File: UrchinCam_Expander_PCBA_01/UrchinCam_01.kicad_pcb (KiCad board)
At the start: 4 copper layers, 31.5 x 65 mm, 86 parts, among them J1 95157-440LF, J2 SM04B-GHS, J3 SM04B-GHS, J4 SM02B-GHS, J5 Conn_01x04_Pin, U1 MP6550, U2 ADS1115IDGS, U3 BNO085, U4 TSR3-2450N, U5 RTL8152B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

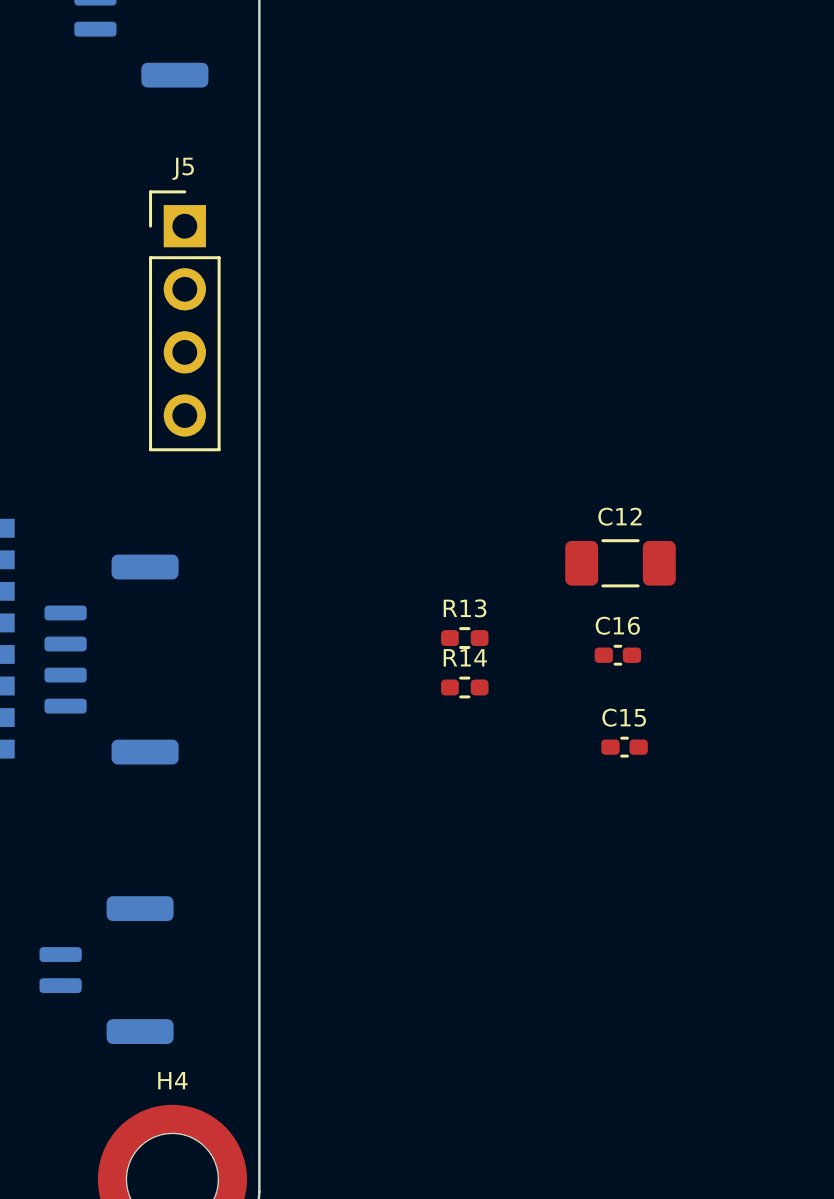
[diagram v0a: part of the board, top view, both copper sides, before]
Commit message: Changed TH USB conn to JST.
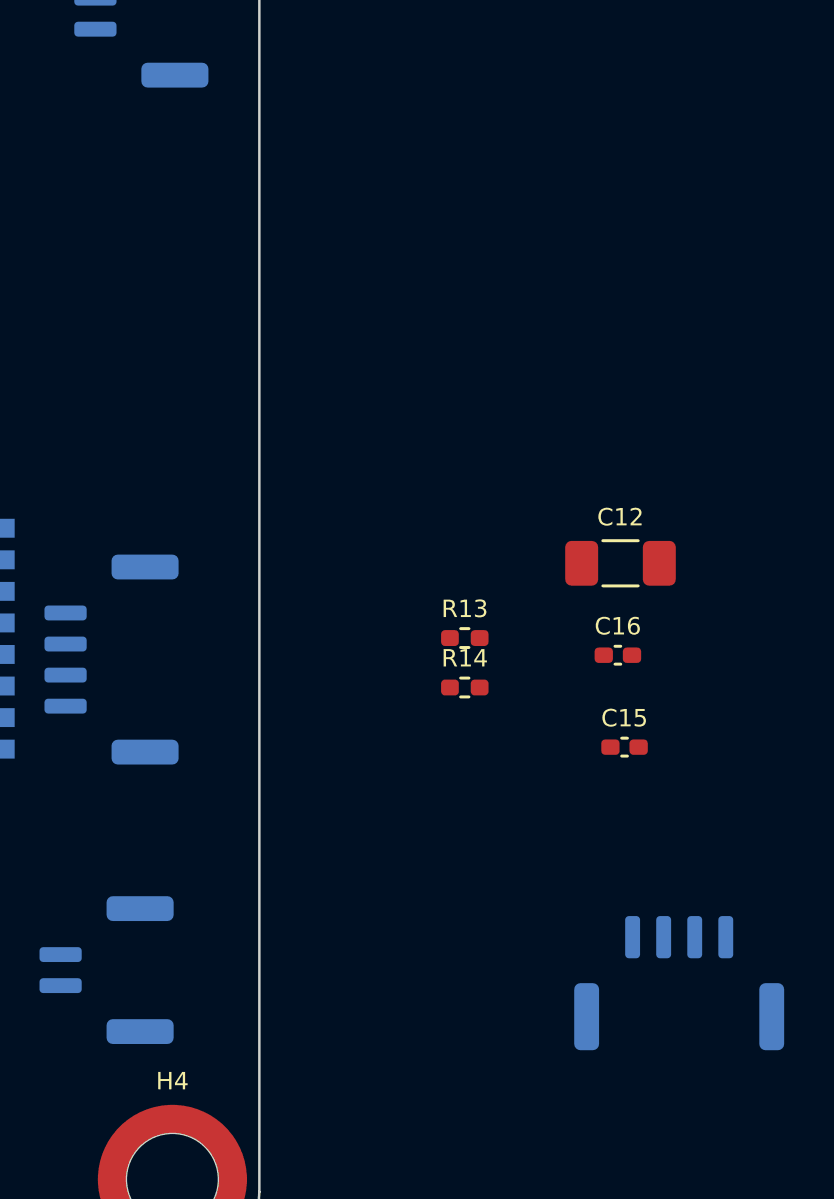
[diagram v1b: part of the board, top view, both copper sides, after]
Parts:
- J5: value Conn_01x04_Pin -> SM04B-GHS; footprint Connector_PinHeader_2.54mm:PinHeader_1x04_P2.54mm_Vertical -> Connector_JST:JST_GH_SM04B-GHS-TB_1x04-1MP_P1.25mm_Horizontal; moved to B.Cu
- moved J5 36.4 mm to (183.4, 124.1), turned to 180 degrees

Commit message: Layout - placing tall components.
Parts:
- added C29: 10uF 50V, Capacitor_SMD:C_0805_2012Metric_Pad1.18x1.45mm_HandSolder, F.Cu at (159.2, 90.3)
- added C30: 10uF 10V, Capacitor_SMD:C_0402_1005Metric_Pad0.74x0.62mm_HandSolder, F.Cu at (158.8, 83.6)
- moved C5 79.0 mm to (116.2, 145.1)
- moved C7 79.0 mm to (115.9, 150.6)
- moved C8 79.0 mm to (128.0, 147.4)
- moved R3 79.0 mm to (119.4, 147.8)
- moved R4 79.0 mm to (131.6, 147.4)
- moved R5 79.0 mm to (134.6, 147.5)
- moved U1 79.0 mm to (119.5, 151.9)
- moved U2 79.0 mm to (129.7, 152.1)
- moved C6 79.0 mm to (116.1, 147.8)
- moved C2 59.6 mm to (158.8, 84.9), turned to 180 degrees
- moved C1 57.3 mm to (156.0, 84.9)
- moved U4 41.4 mm to (155.0, 87.3), turned to -90 degrees
- moved J3 40.4 mm to (162.1, 124.2)
- moved J4 28.0 mm to (162.1, 95.7)
- moved J5 23.5 mm to (162.1, 114.3), turned to -90 degrees
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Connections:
- J2 pad 1: /T+ -> /R-
- J2 pad 2: /T- -> /R+
- J2 pad 3: /R+ -> /T-
- J2 pad 4: /R- -> /T+
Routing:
- net +5V: track 0.00 -> 44.7 mm
- net Net-(J4-Pin_1): track 0.00 -> 16.2 mm, vias 0 -> 2
- net /R-: track 0.00 -> 13.0 mm
- net /R+: track 0.00 -> 11.3 mm
- net /T-: track 0.00 -> 10.2 mm
- net /T+: track 0.00 -> 6.80 mm
- net GND: track 0.00 -> 6.79 mm, vias 0 -> 2

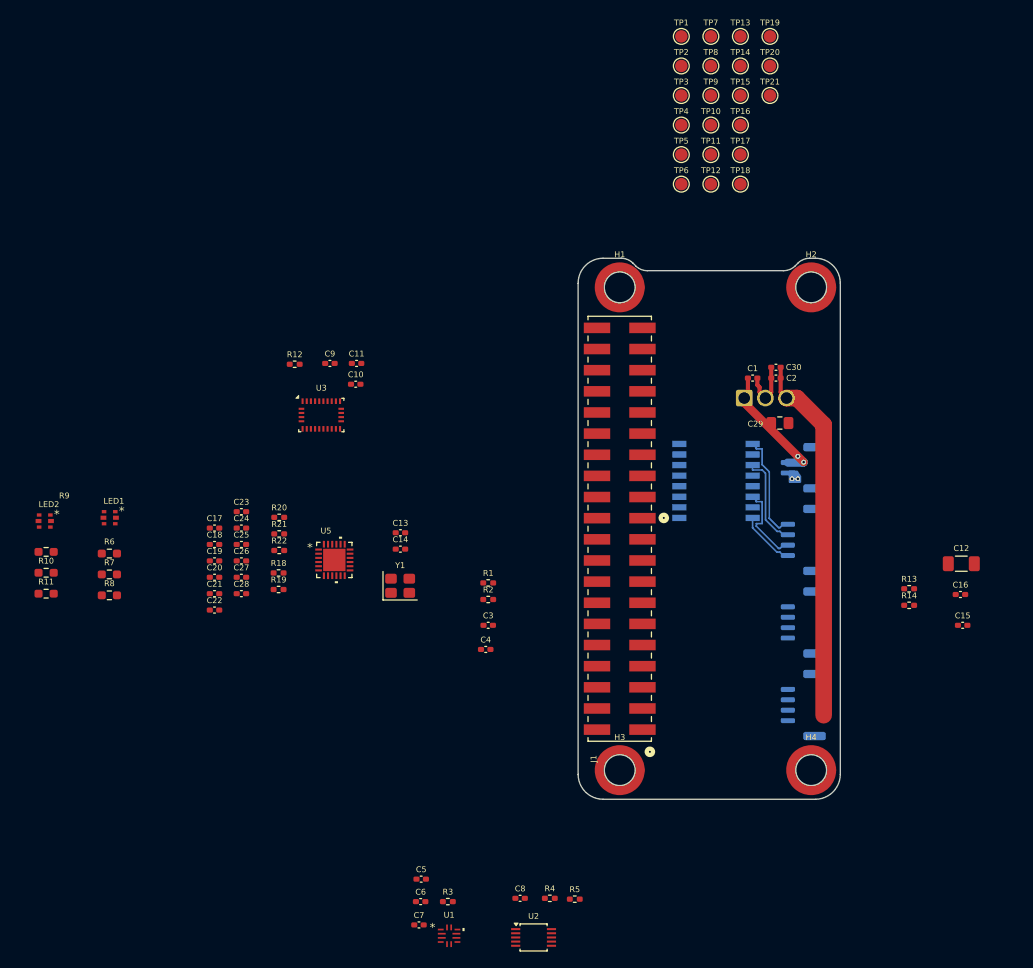
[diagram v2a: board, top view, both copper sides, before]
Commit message: Layout - routing ethernet + magnetics.
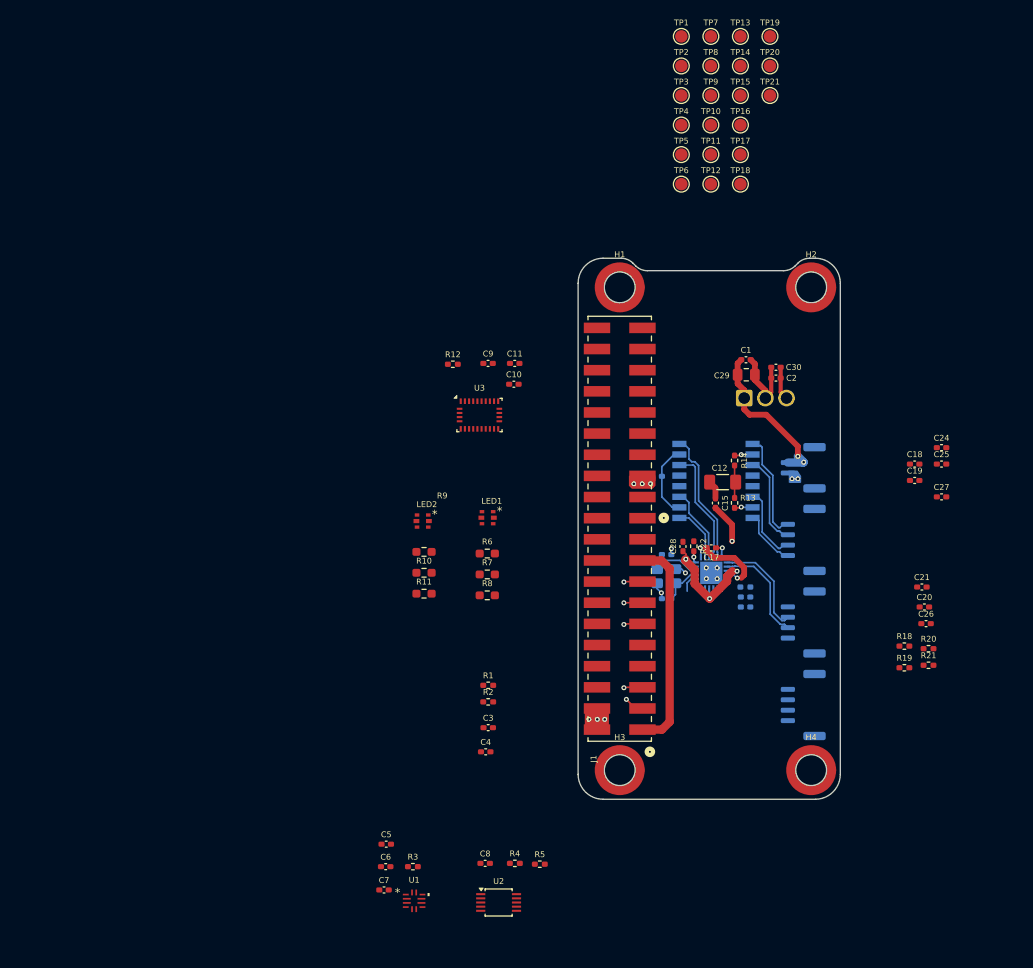
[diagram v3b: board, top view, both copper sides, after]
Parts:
- added FB1: 120Ω @ 100MHz, Resistor_SMD:R_0402_1005Metric_Pad0.72x0.64mm_HandSolder, B.Cu at (155.1, 110.0)
- C13, C14, C16, C22, C23, U5, Y1: moved to B.Cu
- moved C20 85.4 mm to (176.6, 112.4)
- moved C21 85.0 mm to (176.3, 110.0)
- moved C18 84.7 mm to (175.4, 95.2)
- moved C19 84.7 mm to (175.4, 97.2)
- moved C24 84.7 mm to (178.7, 93.3)
- moved C25 84.7 mm to (178.7, 95.2)
- moved C27 84.7 mm to (178.7, 99.2)
- moved C26 82.6 mm to (176.8, 114.4)
- moved R20 79.6 mm to (177.1, 117.4)
- moved R21 79.6 mm to (177.1, 119.4)
- moved R19 75.8 mm to (174.2, 119.7)
- moved R18 75.7 mm to (174.2, 117.1)
- moved C22 63.8 mm to (155.1, 112.4)
- moved C23 61.4 mm to (155.1, 111.2)
- moved C17 59.7 mm to (151.0, 105.3), turned to 180 degrees
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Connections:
- C22 pad 1: +5V -> Net-(U5-VDD5)
- C23 pad 1: +5V -> Net-(U5-VDD5)
- U5 pad 11: +5V -> Net-(U5-VDD5)
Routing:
- net +5V: track 44.7 -> 75.0 mm, vias 0 -> 3
- net +3V3: track 0.00 -> 25.7 mm
- net /VDD10: track 0.00 -> 16.2 mm, vias 0 -> 3
- net /MDI1_N: track 0.00 -> 16.0 mm
- net GND: track 6.79 -> 21.3 mm, vias 2 -> 14
- net /MDI1_P: track 0.00 -> 13.8 mm
- net /USB_P: track 0.00 -> 12.6 mm
- net /USB_N: track 0.00 -> 12.6 mm
- net VDD33: track 0.00 -> 10.8 mm, vias 0 -> 2
- net /MDI0_N: track 0.00 -> 9.01 mm
- net Net-(C16-Pad1): track 0.00 -> 8.96 mm
- net /MDI0_P: track 0.00 -> 6.68 mm
- net /XTAL2: track 0.00 -> 6.49 mm
- net /XTAL1: track 0.00 -> 4.88 mm
- net Net-(C12-Pad1): track 0.00 -> 4.01 mm
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
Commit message: All components except test points positioned.
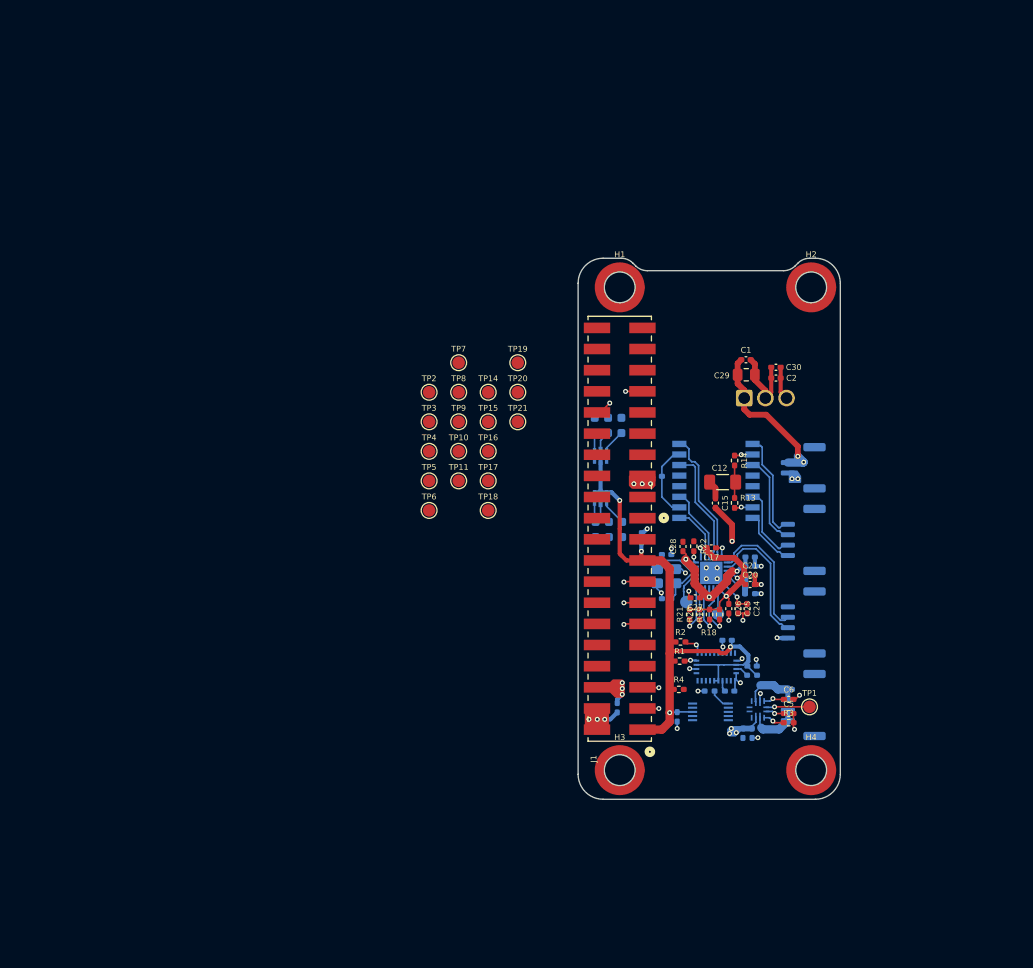
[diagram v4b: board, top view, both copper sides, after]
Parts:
- added C31: 100nF 50V, Capacitor_SMD:C_0402_1005Metric_Pad0.74x0.62mm_HandSolder, B.Cu at (154.8, 127.6)
- C10, C11, C18, C19, C3, C4, C7, C8, C9, LED1, LED2, R10, R11, R12, R5, R6, R7, R8, R9, TP12, TP13, U1, U2, U3: moved to B.Cu
- moved TP1 82.0 mm to (162.8, 124.4)
- moved TP13 68.3 mm to (148.0, 111.8), turned to 180 degrees
- moved C6 52.4 mm to (160.3, 123.5)
- moved R12 51.8 mm to (155.9, 120.6), turned to 180 degrees
- moved TP12 51.6 mm to (151.8, 113.2), turned to 180 degrees
- moved C5 50.8 mm to (160.3, 125.2)
- moved TP21 49.5 mm to (127.8, 90.2)
- moved TP3 49.5 mm to (117.1, 90.2)
- moved TP4 49.5 mm to (117.1, 93.7)
- moved TP5 49.5 mm to (117.1, 97.2)
- moved TP15 49.5 mm to (124.2, 90.2)
- moved TP16 49.5 mm to (124.2, 93.7)
- moved TP17 49.5 mm to (124.2, 97.2)
- moved TP19 49.5 mm to (127.8, 83.0)
- moved TP2 49.5 mm to (117.1, 86.6)
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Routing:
- net +3V3: track 25.7 -> 70.8 mm, vias 0 -> 4
- net +5V: track 75.0 -> 108.7 mm, vias 3 -> 7
- net GND: track 21.3 -> 47.7 mm, vias 14 -> 35
- net VDD33: track 10.8 -> 22.2 mm, vias 2 -> 3
- net Net-(J3-Pin_1): track 0.00 -> 6.94 mm
- net Net-(J3-Pin_3): track 0.00 -> 6.35 mm
- net Net-(U5-LANWAKEB): track 0.00 -> 6.32 mm, vias 0 -> 1
- net Net-(U5-LED0/SPICSB): track 0.00 -> 6.23 mm, vias 0 -> 1
- net Net-(U5-LED1/SPISCK): track 0.00 -> 5.66 mm, vias 0 -> 1
- net Net-(U5-SPISDI/XTALDET): track 0.00 -> 5.37 mm, vias 0 -> 1
- net Net-(U1-~{SLEEP_LDO}): track 0.00 -> 5.23 mm, vias 0 -> 1
- net Net-(U5-VDD5): track 0.00 -> 4.70 mm
- net /VDD10_UPS: track 0.00 -> 4.13 mm, vias 0 -> 1
- net /USB_P: track 12.6 -> 16.2 mm
- net /USB_N: track 12.6 -> 16.1 mm
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
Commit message: Routing done!
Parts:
- TP1, TP10, TP11, TP14, TP15, TP16, TP17, TP18, TP19, TP2, TP20, TP21, TP3, TP4, TP5, TP6, TP7, TP8, TP9: moved to B.Cu
- moved TP8 56.2 mm to (154.5, 131.5), turned to 180 degrees
- moved TP7 54.5 mm to (145.5, 131.5), turned to 180 degrees
- moved TP5 53.0 mm to (157.5, 131.5), turned to 180 degrees
- moved TP10 48.8 mm to (151.5, 131.5), turned to 180 degrees
- moved TP6 43.9 mm to (148.5, 131.5), turned to 180 degrees
- moved TP11 41.4 mm to (157.0, 117.0), turned to 180 degrees
- moved TP4 31.0 mm to (146.5, 84.0), turned to 180 degrees
- moved TP3 30.3 mm to (144.5, 103.0), turned to 180 degrees
- moved TP2 30.0 mm to (146.5, 80.5), turned to 180 degrees
- moved TP9 28.3 mm to (138.0, 112.5), turned to 180 degrees
- moved TP15 24.7 mm to (139.5, 109.5), turned to 180 degrees
- moved TP17 24.3 mm to (146.5, 87.5), turned to 180 degrees
- moved TP14 24.2 mm to (138.0, 106.5), turned to 180 degrees
- moved TP18 22.2 mm to (142.0, 87.5), turned to 180 degrees
- moved TP16 20.3 mm to (144.5, 94.0), turned to 180 degrees
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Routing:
- net /PI_GPIO12: track 2.00 -> 62.4 mm, vias 1 -> 3
- net /PI_GPIO13: track 2.04 -> 59.0 mm, vias 1 -> 3
- net /PI_GPIO5: track 0.00 -> 52.9 mm, vias 0 -> 3
- net Net-(U2-ALERT/RDY): track 0.00 -> 14.7 mm, vias 0 -> 1
- net /I2C_SDA: track 4.47 -> 18.8 mm
- net GND: track 47.7 -> 60.2 mm, vias 35 -> 45
- net /PI_GPIO17: track 2.26 -> 14.7 mm
- net /IMU_INT: track 0.00 -> 12.1 mm, vias 0 -> 2
- net /PI_GPIO26: track 0.00 -> 12.1 mm, vias 0 -> 1
- net /PI_GPIO19: track 0.00 -> 11.8 mm, vias 0 -> 1
- net /PI_GPIO27: track 2.24 -> 11.8 mm
- net /PI_GPIO6: track 0.00 -> 9.32 mm, vias 0 -> 2
- net /I2C_SCL: track 3.47 -> 12.3 mm
- net Net-(U2-AIN1): track 0.00 -> 8.46 mm
- net Net-(U2-AIN3): track 0.00 -> 7.86 mm, vias 0 -> 2
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- added copper zone on In1.Cu, net GND

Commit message: First pass complete!
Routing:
- net +3V3: track 75.3 -> 76.8 mm
- net /T-: track 9.13 -> 8.40 mm
- net /R-: track 13.1 -> 12.4 mm
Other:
- board text added: "3V3"
- board text added: "5V"
- board text added: "ETH"
- board text added: "GND"
- board text added: "MOTOR"
- board text added: "USB"
- board text added: "VIN"
